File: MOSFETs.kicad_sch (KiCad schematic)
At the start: 13 parts, among them Q1 IRF3205, Q2 IRF3205, Q3 IRF3205, Q4 IRF3205, Q5 IRF3205, Q6 IRF3205

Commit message: Add proper JST Connector
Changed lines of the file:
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@@
     (stroke (width 0) (type default))
+  )
+  (global_label "PWR_SRC" (shape input) (at 83.82 44.45 180) (fields_autoplaced)
+    (effects (font (size 1.27 1.27)) (justify right))
+    (property "Intersheetrefs" "${INTERSHEET_REFS}" (at 72.2057 44.45 0)
+      (effects (font (size 1.27 1.27)) (justify right) hide)
+    )
+  )
+  (global_label "PWR_SRC" (shape input) (at 86.36 66.04 180) (fields_autoplaced)
+    (effects (font (size 1.27 1.27)) (justify right))
+    (property "Intersheetrefs" "${INTERSHEET_REFS}" (at 74.7457 66.04 0)
+      (effects (font (size 1.27 1.27)) (justify right) hide)
+    )
   )
   (hierarchical_label "SP2" (shape input) (at 123.19 99.06 180) (fields_autoplaced)
@@
     (effects (font (size 1.27 1.27)) (justify right))
   )
-  (hierarchical_label "PWR_SRC" (shape input) (at 86.36 66.04 180) (fields_autoplaced)
-    (effects (font (size 1.27 1.27)) (justify right))
-  )
   (hierarchical_label "M_L2" (shape input) (at 115.57 73.66 180) (fields_autoplaced)
     (effects (font (size 1.27 1.27)) (justify right))
@@
     (effects (font (size 1.27 1.27)) (justify right))
   )
-  (hierarchical_label "PWR_SRC" (shape input) (at 83.82 44.45 180) (fields_autoplaced)
-    (effects (font (size 1.27 1.27)) (justify right))
-  )

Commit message: fix ERC
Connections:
- net M_H1: now also Q1.1 (G)
- net M_L1: now also Q4.1 (G)
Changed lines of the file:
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@@
+    (stroke (width 0) (type default))
+  )
+  (wire (pts (xy 80.01 73.66) (xy 82.55 73.66))
     (stroke (width 0) (type default))
   )
@@
     (stroke (width 0) (type default))
   )
+  (wire (pts (xy 80.01 88.9) (xy 82.55 88.9))
+    (stroke (width 0) (type default))
+  )

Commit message: Fixed stuff
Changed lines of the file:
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@@
     (stroke (width 0) (type default))
   )
-  (wire (pts (xy 86.36 99.06) (xy 90.17 99.06))
+  (wire (pts (xy 87.63 99.06) (xy 90.17 99.06))
     (stroke (width 0) (type default))
   )
@@
     (stroke (width 0) (type default))
   )
-  (wire (pts (xy 86.36 110.49) (xy 90.17 110.49))
+  (wire (pts (xy 87.63 110.49) (xy 90.17 110.49))
     (stroke (width 0) (type default))
   )
@@
     (effects (font (size 1.27 1.27)) (justify right))
   )
-  (hierarchical_label "SP1" (shape input) (at 86.36 99.06 180) (fields_autoplaced)
+  (hierarchical_label "SP1" (shape input) (at 87.63 99.06 180) (fields_autoplaced)
     (effects (font (size 1.27 1.27)) (justify right))
   )
@@
     (effects (font (size 1.27 1.27)) (justify right))
   )
-  (hierarchical_label "SN1" (shape input) (at 86.36 110.49 180) (fields_autoplaced)
+  (hierarchical_label "SN1" (shape input) (at 87.63 110.49 180) (fields_autoplaced)
     (effects (font (size 1.27 1.27)) (justify right))
   )

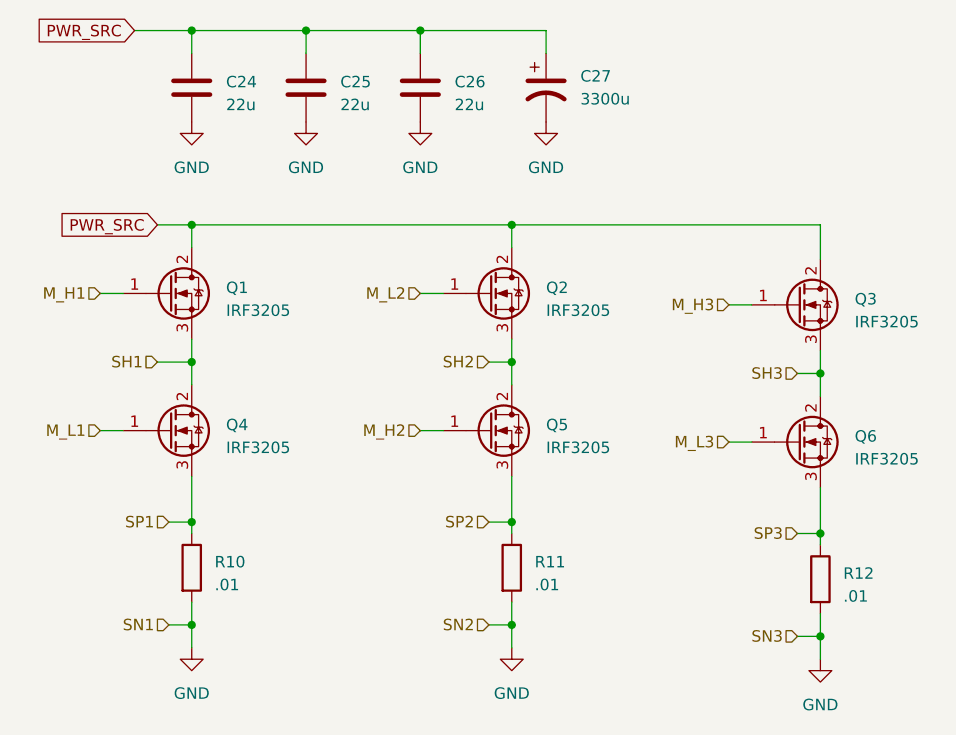
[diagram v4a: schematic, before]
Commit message: Switch M_H2 and M_L2
Wrong gate pins were connected
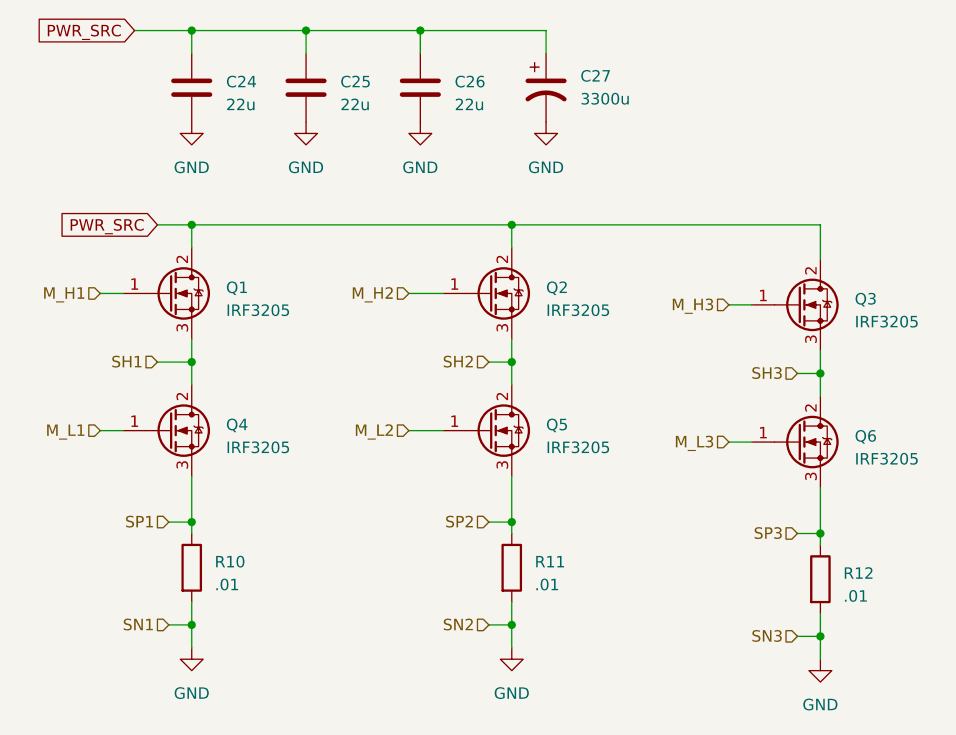
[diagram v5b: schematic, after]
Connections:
- net M_H2: now also Q2.1 (G); no longer Q5.1 (G)
- net M_L2: now also Q5.1 (G); no longer Q2.1 (G)
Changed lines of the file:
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@@
-    (stroke (width 0) (type default))
-  )
-  (wire (pts (xy 115.57 73.66) (xy 118.11 73.66))
     (stroke (width 0) (type default))
   )
@@
   )
   (wire (pts (xy 90.17 66.04) (xy 125.73 66.04))
-    (stroke (width 0) (type default))
-  )
-  (wire (pts (xy 115.57 88.9) (xy 118.11 88.9))
     (stroke (width 0) (type default))
   )
@@
     (stroke (width 0) (type default))
   )
+  (wire (pts (xy 114.3 88.9) (xy 118.11 88.9))
+    (stroke (width 0) (type default))
+  )
   (wire (pts (xy 90.17 99.06) (xy 90.17 100.33))
     (stroke (width 0) (type default))
@@
   )
   (wire (pts (xy 125.73 99.06) (xy 125.73 100.33))
+    (stroke (width 0) (type default))
+  )
+  (wire (pts (xy 114.3 73.66) (xy 118.11 73.66))
     (stroke (width 0) (type default))
   )
@@
     (effects (font (size 1.27 1.27)) (justify right))
   )
-  (hierarchical_label "M_L2" (shape input) (at 115.57 73.66 180) (fields_autoplaced)
+  (hierarchical_label "M_L2" (shape input) (at 114.3 88.9 180) (fields_autoplaced)
     (effects (font (size 1.27 1.27)) (justify right))
   )
-  (hierarchical_label "M_H2" (shape input) (at 115.57 88.9 180) (fields_autoplaced)
+  (hierarchical_label "M_H2" (shape input) (at 114.3 73.66 180) (fields_autoplaced)
     (effects (font (size 1.27 1.27)) (justify right))
   )
